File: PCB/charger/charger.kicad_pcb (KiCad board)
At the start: 2 copper layers, 26.9 x 17 mm, 18 parts, among them J1 Conn_01x02_Socket, J2 USB_C_Receptacle, J3 Conn_01x02_Socket, J4 Conn_01x02_Socket, J5 Conn_01x02_Socket, Q2 BSS83P, U1 MCP73831T-2ACI/OT

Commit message: idk
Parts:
- D1, D2: footprint LED_SMD:LED_0402_1005Metric -> LED_SMD:LED_0603_1608Metric
- J3, J4, J5: moved to B.Cu
- moved R2 19.1 mm to (73.7, 73.4)
- moved J1 18.9 mm to (74.6, 80.2)
- moved R6 18.8 mm to (80.1, 73.8)
- moved R3 18.8 mm to (75.2, 73.6)
- moved D2 18.7 mm to (75.0, 76.1)
- moved D3 18.5 mm to (77.6, 76.0)
- moved D1 18.5 mm to (71.2, 73.2)
- moved J3 18.4 mm to (70.1, 84.6), turned to 180 degrees
- moved J2 18.4 mm to (65.3, 77.9)
- moved J4 18.4 mm to (88.5, 84.6), turned to 180 degrees
- moved J5 18.4 mm to (84.0, 71.6), turned to 180 degrees
- moved Q2 18.4 mm to (77.7, 81.3)
- moved R1 18.4 mm to (71.0, 80.7)
- moved R5 18.4 mm to (71.5, 79.2)
- moved R4 18.4 mm to (70.6, 79.3)
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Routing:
- net GND: track 23.2 -> 2.32 mm, vias 5 -> 7
- net VOUT: track 14.6 -> 11.2 mm
- net 5V: track 31.1 -> 34.0 mm
- net Net-(U1-PROG): track 1.53 -> 0.00 mm
- net Net-(U1-STAT): track 7.46 -> 8.50 mm
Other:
- board size 26.9 x 17 mm -> 27.2 x 16.6 mm

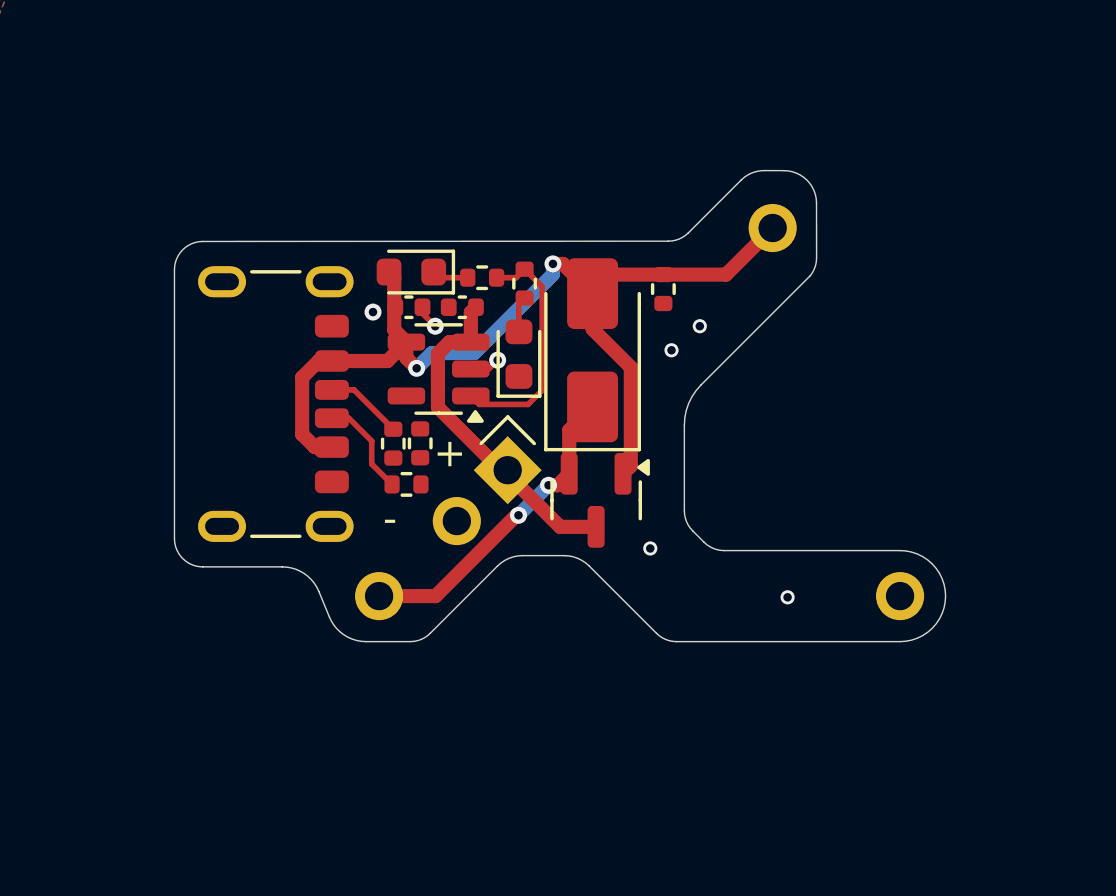
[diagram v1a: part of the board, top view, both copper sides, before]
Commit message: reorganizing repo
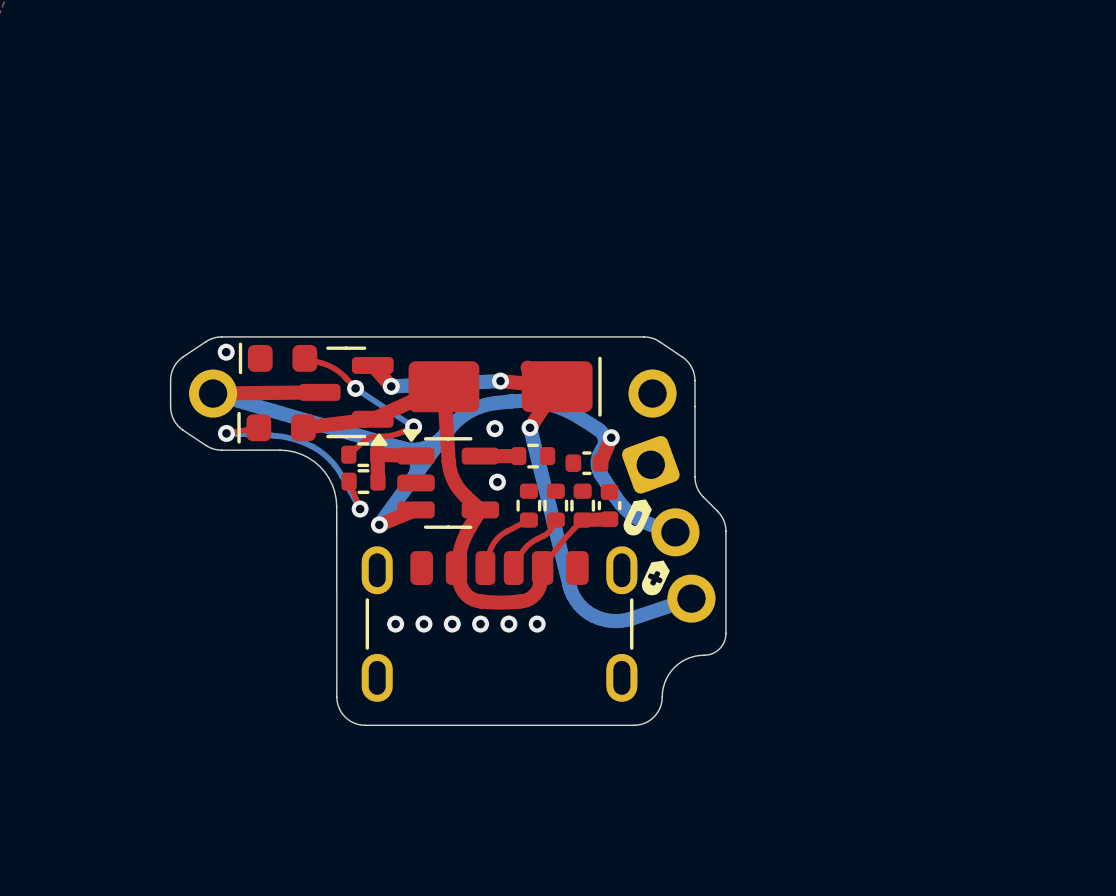
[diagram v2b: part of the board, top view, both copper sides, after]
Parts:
- added REF**: Tab, PCM_kikit:Tab, F.Cu at (68.3, 84.9)
- added REF**: Tab, PCM_kikit:Tab, F.Cu at (74.5, 75.4)
- added kibuzzard-676F29EF: G***, kibuzzard-676F29EF, F.Cu at (79.8, 84.0)
- added kibuzzard-676F2A21: G***, kibuzzard-676F2A21, F.Cu at (79.2, 81.8)
- added kibuzzard-6770932C: G***, kibuzzard-6770932C, B.Cu at (76.4, 77.5)
- added kibuzzard-6770936F: G***, kibuzzard-6770936F, B.Cu at (74.3, 87.6)
- added kibuzzard-6770A330: G***, kibuzzard-6770A330, B.Cu at (67.0, 77.6)
- added kibuzzard-6770A34A: G***, kibuzzard-6770A34A, B.Cu at (78.2, 85.8)
- added kibuzzard-6770A35D: G***, kibuzzard-6770A35D, B.Cu at (78.0, 81.9)
- added kibuzzard-6770A364: G***, kibuzzard-6770A364, B.Cu at (76.3, 80.2)
- R5: value 10K\ -> 20K
- moved J5 20.6 mm to (64.2, 77.5), turned to -90 degrees
- moved J2 12.6 mm to (74.3, 86.7), turned to 0 degrees
- moved J4 11.3 mm to (79.7, 77.5)
- moved J3 11.0 mm to (81.1, 84.7), turned to -90 degrees
- moved C1 9.97 mm to (78.2, 81.5), turned to 90 degrees
- moved Q2 9.61 mm to (68.9, 77.5), turned to 180 degrees
- moved D2 8.35 mm to (66.7, 76.2), turned to 0 degrees
- moved R2 8.33 mm to (69.5, 80.6)
- moved R3 8.30 mm to (69.5, 79.7), turned to 0 degrees
- moved R6 8.16 mm to (77.2, 81.5), turned to -90 degrees
- moved D1 7.17 mm to (66.6, 78.7), turned to 0 degrees
- moved C2 7.05 mm to (77.4, 80.0)
- moved R1 5.33 mm to (76.3, 81.5), turned to -90 degrees
- moved R4 5.26 mm to (75.3, 81.5), turned to -90 degrees
- moved J1 5.06 mm to (79.7, 80.0), turned to 20 degrees
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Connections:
- J5 pad 1: 5V -> VBATT
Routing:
- net VBATT: track 12.6 -> 31.5 mm, vias 0 -> 2
- net 5V: track 34.0 -> 19.9 mm, vias 2 -> 0
- net VOUT: track 11.2 -> 20.6 mm, vias 2 -> 3
- net Net-(D1-K): track 1.27 -> 8.12 mm, vias 0 -> 2
- net Net-(U1-STAT): track 8.50 -> 2.30 mm
- net Net-(D2-A): track 1.28 -> 7.16 mm, vias 0 -> 2
- net GND: track 2.32 -> 0.00 mm, vias 7 -> 9
- net Net-(U1-PROG): track 0.00 -> 1.35 mm
- net CC2: track 3.57 -> 2.32 mm
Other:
- board size 27.2 x 16.6 mm -> 19.6 x 13.7 mm
- board text removed: "+"
- board text removed: "-"
